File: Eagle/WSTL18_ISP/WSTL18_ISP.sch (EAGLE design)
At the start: 2 parts, among them J3 FEMALE 2x3

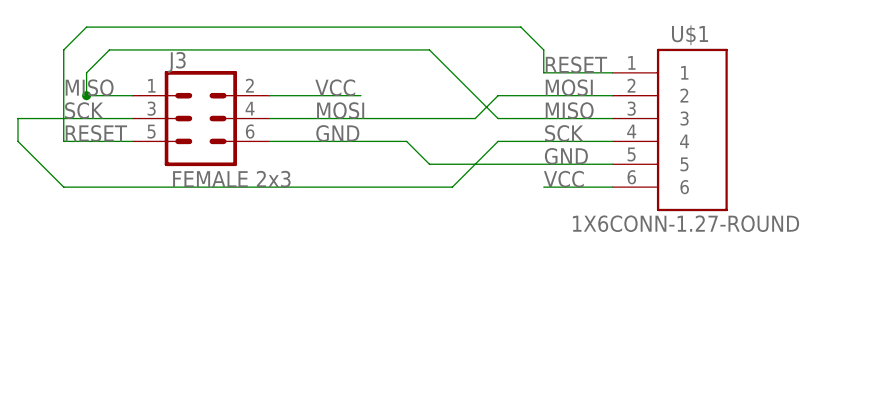
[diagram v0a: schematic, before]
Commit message: Finished design of WSTL18 in-system programming adaptor
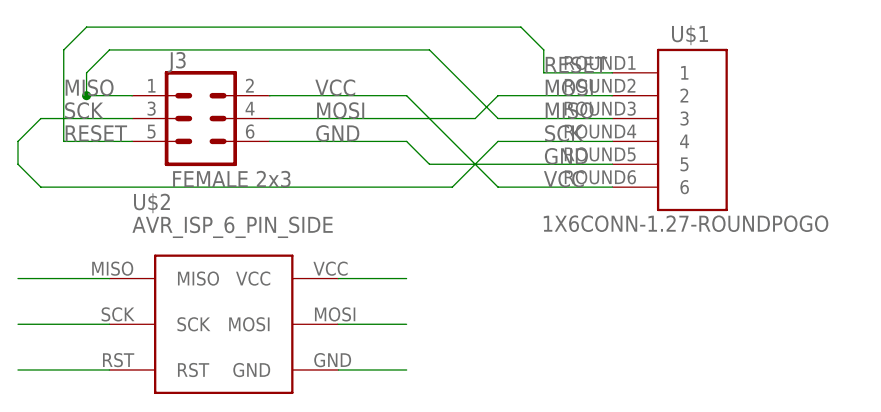
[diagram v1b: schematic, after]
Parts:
- added U$2: AVR_ISP_6_PIN_SIDE, Connectors:AVR_ISP_6_PIN_SIDE
- U$1: value 1X6CONN-1.27-ROUND -> 1X6CONN-1.27-ROUNDPOGO; device AVR_ISP_127:1X6CONN-1.27-ROUND -> AVR_ISP_127:1X6CONN-1.27-ROUNDPOGO
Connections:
- net GND: now also U$2.GND
- net MISO: now also U$2.MISO
- net MOSI: now also U$2.MOSI
- net RESET: now also U$2.RST
- net SCK: now also U$2.SCK
- net VCC: now also U$2.VCC
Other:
- moved on the sheet: U$1
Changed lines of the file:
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@@
 <grid distance="0.1" unitdist="inch" unit="inch" style="lines" multiple="1" display="no" altdistance="0.01" altunitdist="inch" altunit="inch"/>
 <layers>
-<layer number="1" name="Top" color="4" fill="1" visible="yes" active="no"/>
-<layer number="16" name="Bottom" color="1" fill="1" visible="yes" active="no"/>
-<layer number="17" name="Pads" color="2" fill="1" visible="yes" active="no"/>
-<layer number="18" name="Vias" color="2" fill="1" visible="yes" active="no"/>
-<layer number="19" name="Unrouted" color="6" fill="1" visible="yes" active="no"/>
-<layer number="20" name="Dimension" color="15" fill="1" visible="yes" active="no"/>
-<layer number="21" name="tPlace" color="7" fill="1" visible="yes" active="no"/>
-<layer number="22" name="bPlace" color="7" fill="1" visible="yes" active="no"/>
-<layer number="23" name="tOrigins" color="15" fill="1" visible="yes" active="no"/>
-<layer number="24" name="bOrigins" color="15" fill="1" visible="yes" active="no"/>
-<layer number="25" name="tNames" color="7" fill="1" visible="yes" active="no"/>
-<layer number="26" name="bNames" color="7" fill="1" visible="yes" active="no"/>
-<layer number="27" name="tValues" color="7" fill="1" visible="yes" active="no"/>
-<layer number="28" name="bValues" color="7" fill="1" visible="yes" active="no"/>
+<layer number="1" name="Top" color="4" fill="1" visible="no" active="no"/>
+<layer number="16" name="Bottom" color="1" fill="1" visible="no" active="no"/>
+<layer number="17" name="Pads" color="2" fill="1" visible="no" active="no"/>
+<layer number="18" name="Vias" color="2" fill="1" visible="no" active="no"/>
+<layer number="19" name="Unrouted" color="6" fill="1" visible="no" active="no"/>
+<layer number="20" name="Dimension" color="15" fill="1" visible="no" active="no"/>
+<layer number="21" name="tPlace" color="7" fill="1" visible="no" active="no"/>
+<layer number="22" name="bPlace" color="7" fill="1" visible="no" active="no"/>
+<layer number="23" name="tOrigins" color="15" fill="1" visible="no" active="no"/>
+<layer number="24" name="bOrigins" color="15" fill="1" visible="no" active="no"/>
+<layer number="25" name="tNames" color="7" fill="1" visible="no" active="no"/>
+<layer number="26" name="bNames" color="7" fill="1" visible="no" active="no"/>
+<layer number="27" name="tValues" color="7" fill="1" visible="no" active="no"/>
+<layer number="28" name="bValues" color="7" fill="1" visible="no" active="no"/>
 <layer number="29" name="tStop" color="7" fill="3" visible="no" active="no"/>
 <layer number="30" name="bStop" color="7" fill="6" visible="no" active="no"/>
@@
 <layer number="35" name="tGlue" color="7" fill="4" visible="no" active="no"/>
 <layer number="36" name="bGlue" color="7" fill="5" visible="no" active="no"/>
-<layer number="37" name="tTest" color="7" fill="1" visible="yes" active="no"/>
-<layer number="38" name="bTest" color="7" fill="1" visible="yes" active="no"/>
+<layer number="37" name="tTest" color="7" fill="1" visible="no" active="no"/>
+<layer number="38" name="bTest" color="7" fill="1" visible="no" active="no"/>
 <layer number="39" name="tKeepout" color="4" fill="11" visible="no" active="no"/>
 <layer number="40" name="bKeepout" color="1" fill="11" visible="no" active="no"/>
@@
 <layer number="44" name="Drills" color="7" fill="1" visible="no" active="no"/>
 <layer number="45" name="Holes" color="7" fill="1" visible="no" active="no"/>
-<layer number="46" name="Milling" color="3" fill="1" visible="yes" active="no"/>
-<layer number="47" name="Measures" color="7" fill="1" visible="yes" active="no"/>
-<layer number="48" name="Document" color="7" fill="1" visible="yes" active="no"/>
-<layer number="49" name="Reference" color="7" fill="1" visible="yes" active="no"/>
-<layer number="50" name="dxf" color="7" fill="1" visible="yes" active="no"/>
-<layer number="51" name="tDocu" color="7" fill="1" visible="yes" active="no"/>
-<layer number="52" name="bDocu" color="7" fill="1" visible="yes" active="no"/>
-<layer number="53" name="tGND_GNDA" color="7" fill="9" visible="yes" active="no"/>
-<layer number="54" name="bGND_GNDA" color="1" fill="9" visible="yes" active="no"/>
-<layer number="56" name="wert" color="7" fill="1" visible="yes" active="no"/>
-<layer number="57" name="tCAD" color="7" fill="1" visible="yes" active="no"/>
-<layer number="59" name="tCarbon" color="7" fill="1" visible="yes" active="no"/>
-<layer number="60" name="bCarbon" color="7" fill="1" visible="yes" active="no"/>
+<layer number="46" name="Milling" color="3" fill="1" visible="no" active="no"/>
+<layer number="47" name="Measures" color="7" fill="1" visible="no" active="no"/>
+<layer number="48" name="Document" color="7" fill="1" visible="no" active="no"/>
+<layer number="49" name="Reference" color="7" fill="1" visible="no" active="no"/>
+<layer number="50" name="dxf" color="7" fill="1" visible="no" active="no"/>
+<layer number="51" name="tDocu" color="7" fill="1" visible="no" active="no"/>
+<layer number="52" name="bDocu" color="7" fill="1" visible="no" active="no"/>
+<layer number="53" name="tGND_GNDA" color="7" fill="9" visible="no" active="no"/>
+<layer number="54" name="bGND_GNDA" color="1" fill="9" visible="no" active="no"/>
+<layer number="56" name="wert" color="7" fill="1" visible="no" active="no"/>
+<layer number="57" name="tCAD" color="7" fill="1" visible="no" active="no"/>
+<layer number="59" name="tCarbon" color="7" fill="1" visible="no" active="no"/>
+<layer number="60" name="bCarbon" color="7" fill="1" visible="no" active="no"/>
 <layer number="90" name="Modules" color="5" fill="1" visible="yes" active="yes"/>
 <layer number="91" name="Nets" color="2" fill="1" visible="yes" active="yes"/>
@@
 <parts>
 <part name="J3" library="SparkFun-Connectors" deviceset="CONN_03X2" device="FEMALE" value="FEMALE 2x3"/>
-<part name="U$1" library="AVR_ISP_127" deviceset="1X6CONN-1.27-ROUND" device=""/>
+<part name="U$1" library="AVR_ISP_127" deviceset="1X6CONN-1.27-ROUNDPOGO" device=""/>
+<part name="U$2" library="Connectors" deviceset="AVR_ISP_6_PIN_SIDE" device=""/>
 </parts>
 <sheets>
@@
 <instance part="J3" gate="G$1" x="17.78" y="33.02"/>
 <instance part="U$1" gate="G$1" x="73.66" y="35.56"/>
+<instance part="U$2" gate="G$1" x="22.86" y="10.16"/>
 </instances>
 <busses>
@@
 <segment>
 <pinref part="U$1" gate="G$1" pin="6"/>
-<wire x1="63.5" y1="25.4" x2="55.88" y2="25.4" width="0.1524" layer="91"/>
+<wire x1="63.5" y1="25.4" x2="50.8" y2="25.4" width="0.1524" layer="91"/>
 <label x="55.88" y="25.4" size="1.778" layer="95" font="vector"/>
-</segment>
-<segment>
+<wire x1="50.8" y1="25.4" x2="40.64" y2="35.56" width="0.1524" layer="91"/>
 <pinref part="J3" gate="G$1" pin="2"/>
-<wire x1="25.4" y1="35.56" x2="35.56" y2="35.56" width="0.1524" layer="91"/>
+<wire x1="25.4" y1="35.56" x2="40.64" y2="35.56" width="0.1524" layer="91"/>
 <label x="30.48" y="35.56" size="1.778" layer="95" font="vector"/>
+</segment>
+<segment>
+<pinref part="U$2" gate="G$1" pin="VCC"/>
+<wire x1="33.02" y1="15.24" x2="40.64" y2="15.24" width="0.1524" layer="91"/>
 </segment>
 </net>
@@
 <wire x1="25.4" y1="30.48" x2="40.64" y2="30.48" width="0.1524" layer="91"/>
 <label x="30.48" y="30.48" size="1.778" layer="95" font="vector"/>
+</segment>
+<segment>
+<pinref part="U$2" gate="G$1" pin="GND"/>
+<wire x1="33.02" y1="5.08" x2="40.64" y2="5.08" width="0.1524" layer="91"/>
 </segment>
 </net>
@@
 <wire x1="55.88" y1="40.64" x2="55.88" y2="38.1" width="0.1524" layer="91"/>
 </segment>
+<segment>
+<pinref part="U$2" gate="G$1" pin="RST"/>
+<wire x1="7.62" y1="5.08" x2="-2.54" y2="5.08" width="0.1524" layer="91"/>
+</segment>
 </net>
 <net name="MOSI" class="0">
@@
 <label x="55.88" y="35.56" size="1.778" layer="95" font="vector"/>
 </segment>
+<segment>
+<pinref part="U$2" gate="G$1" pin="MOSI"/>
+<wire x1="33.02" y1="10.16" x2="40.64" y2="10.16" width="0.1524" layer="91"/>
+</segment>
 </net>
 <net name="SCK" class="0">
@@
 <label x="55.88" y="30.48" size="1.778" layer="95" font="vector"/>
 <wire x1="50.8" y1="30.48" x2="45.72" y2="25.4" width="0.1524" layer="91"/>
-<wire x1="45.72" y1="25.4" x2="2.54" y2="25.4" width="0.1524" layer="91"/>
-<wire x1="2.54" y1="25.4" x2="-2.54" y2="30.48" width="0.1524" layer="91"/>
-<wire x1="-2.54" y1="30.48" x2="-2.54" y2="33.02" width="0.1524" layer="91"/>
+<wire x1="45.72" y1="25.4" x2="0" y2="25.4" width="0.1524" layer="91"/>
+<wire x1="0" y1="25.4" x2="-2.54" y2="27.94" width="0.1524" layer="91"/>
+<wire x1="-2.54" y1="27.94" x2="-2.54" y2="30.48" width="0.1524" layer="91"/>
+<wire x1="-2.54" y1="30.48" x2="0" y2="33.02" width="0.1524" layer="91"/>
+<wire x1="0" y1="33.02" x2="10.16" y2="33.02" width="0.1524" layer="91"/>
 <pinref part="J3" gate="G$1" pin="3"/>
-<wire x1="10.16" y1="33.02" x2="-2.54" y2="33.02" width="0.1524" layer="91"/>
 <label x="2.54" y="33.02" size="1.778" layer="95" font="vector"/>
+</segment>
+<segment>
+<pinref part="U$2" gate="G$1" pin="SCK"/>
+<wire x1="7.62" y1="10.16" x2="-2.54" y2="10.16" width="0.1524" layer="91"/>
 </segment>
 </net>
@@
 <junction x="5.08" y="35.56"/>
 </segment>
-</net>
+<segment>
+<pinref part="U$2" gate="G$1" pin="MISO"/>
+<wire x1="7.62" y1="15.24" x2="-2.54" y2="15.24" width="0.1524" layer="91"/>
+</segment>
+</net>
